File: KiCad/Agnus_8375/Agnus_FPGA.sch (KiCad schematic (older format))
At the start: 19 parts, among them J6 Conn_01x01, U1 10M02SCU169C8G, U2 LM1117-3.3

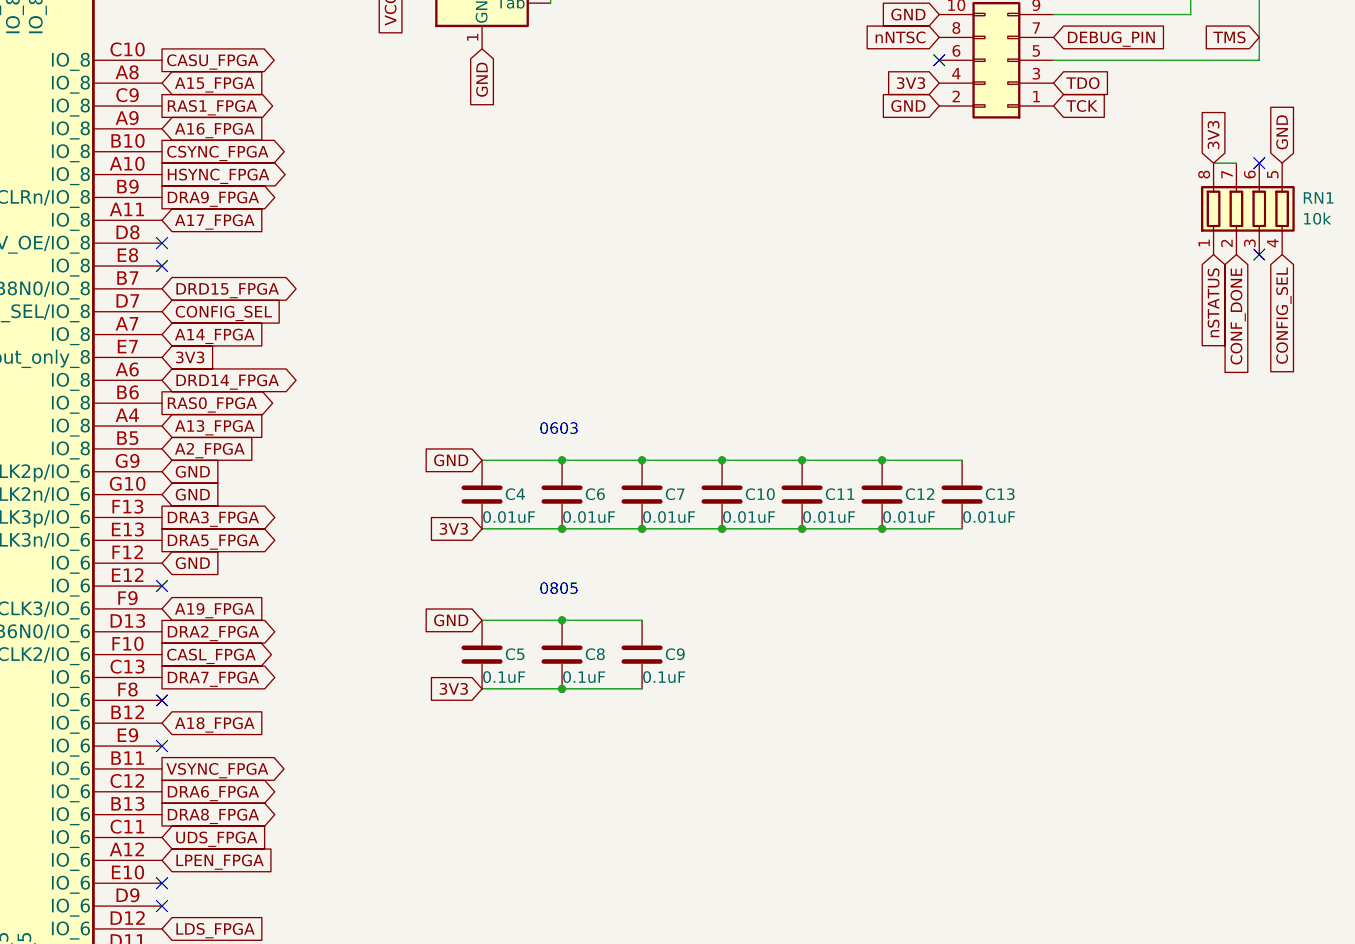
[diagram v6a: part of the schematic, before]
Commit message: Added more decoupling caps, changed to 6 mil copper pour clearance, added some more 3V3/GND vias, improved routing.
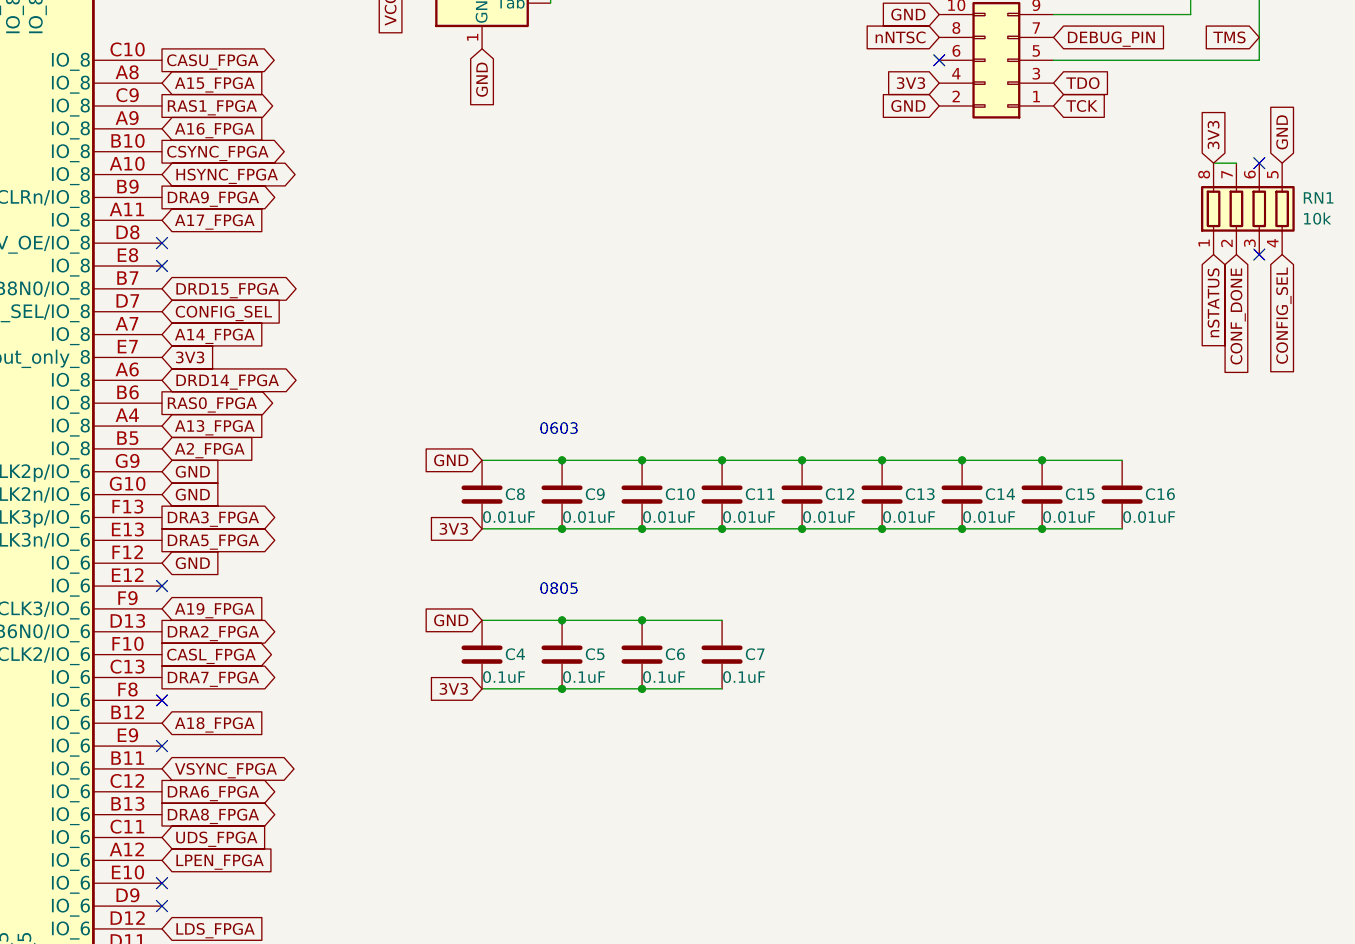
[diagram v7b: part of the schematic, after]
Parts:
- added C10, C13: 0.01uF, Capacitor_SMD:C_0603_1608Metric_Pad1.05x0.95mm_HandSolder, symbol Device:C
- added C6: 0.1uF, Capacitor_SMD:C_0805_2012Metric_Pad1.15x1.40mm_HandSolder, symbol Device:C
- renumbered C7 to C11, C10 to C12, C11 to C14, C12 to C15, C13 to C16, C5 to C4, C8 to C5, C9 to C7, C4 to C8, C6 to C9
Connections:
- net 3V3: now also C10.2, C13.2, C6.2
- net GND: now also C10.1, C13.1, C6.1
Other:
- moved on the sheet: C11, C12, C14, C15, C16, C7
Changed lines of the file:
@@
 Text GLabel 5850 2550 2    50   Input ~ 0
 A17_FPGA
-Text GLabel 5850 4950 2    50   Output ~ 0
+Text GLabel 5850 4950 2    50   BiDi ~ 0
 VSYNC_FPGA
 Text GLabel 5850 2250 2    50   Output ~ 0
 CSYNC_FPGA
-Text GLabel 5850 2350 2    50   Output ~ 0
+Text GLabel 5850 2350 2    50   BiDi ~ 0
 HSYNC_FPGA
 Text GLabel 5850 2150 2    50   Input ~ 0
@@
 L Device:C C?
 U 1 1 60CC8EF6
+P 10050 3750
+AR Path="/60CC8EF6" Ref="C?"  Part="1"
+AR Path="/608A10F5/60CC8EF6" Ref="C16"  Part="1"
+F 0 "C16" H 10150 3750 50  0000 L CNN
+F 1 "0.01uF" H 10050 3650 50  0000 L CNN
+F 2 "Capacitor_SMD:C_0603_1608Metric_Pad1.05x0.95mm_HandSolder" H 10088 3600 50  0001 C CNN
+F 3 "~" H 10050 3750 50  0001 C CNN
+	1    10050 3750
+	1    0    0    -1
+$EndComp
+$Comp
+L Device:C C?
+U 1 1 60CC8EFC
+P 9700 3750
+AR Path="/60CC8EFC" Ref="C?"  Part="1"
+AR Path="/608A10F5/60CC8EFC" Ref="C15"  Part="1"
+F 0 "C15" H 9800 3750 50  0000 L CNN
+F 1 "0.01uF" H 9700 3650 50  0000 L CNN
+F 2 "Capacitor_SMD:C_0603_1608Metric_Pad1.05x0.95mm_HandSolder" H 9738 3600 50  0001 C CNN
+F 3 "~" H 9700 3750 50  0001 C CNN
+	1    9700 3750
+	1    0    0    -1
+$EndComp
+$Comp
+L Device:C C?
+U 1 1 60CC8F02
 P 9350 3750
-AR Path="/60CC8EF6" Ref="C?"  Part="1"
-AR Path="/608A10F5/60CC8EF6" Ref="C13"  Part="1"
-F 0 "C13" H 9450 3750 50  0000 L CNN
+AR Path="/60CC8F02" Ref="C?"  Part="1"
+AR Path="/608A10F5/60CC8F02" Ref="C14"  Part="1"
+F 0 "C14" H 9450 3750 50  0000 L CNN
 F 1 "0.01uF" H 9350 3650 50  0000 L CNN
 F 2 "Capacitor_SMD:C_0603_1608Metric_Pad1.05x0.95mm_HandSolder" H 9388 3600 50  0001 C CNN
@@
 	1    0    0    -1
 $EndComp
-$Comp
-L Device:C C?
-U 1 1 60CC8EFC
-P 9000 3750
-AR Path="/60CC8EFC" Ref="C?"  Part="1"
-AR Path="/608A10F5/60CC8EFC" Ref="C12"  Part="1"
-F 0 "C12" H 9100 3750 50  0000 L CNN
-F 1 "0.01uF" H 9000 3650 50  0000 L CNN
-F 2 "Capacitor_SMD:C_0603_1608Metric_Pad1.05x0.95mm_HandSolder" H 9038 3600 50  0001 C CNN
-F 3 "~" H 9000 3750 50  0001 C CNN
-	1    9000 3750
-	1    0    0    -1
-$EndComp
-$Comp
-L Device:C C?
-U 1 1 60CC8F02
-P 8650 3750
-AR Path="/60CC8F02" Ref="C?"  Part="1"
-AR Path="/608A10F5/60CC8F02" Ref="C11"  Part="1"
-F 0 "C11" H 8750 3750 50  0000 L CNN
-F 1 "0.01uF" H 8650 3650 50  0000 L CNN
-F 2 "Capacitor_SMD:C_0603_1608Metric_Pad1.05x0.95mm_HandSolder" H 8688 3600 50  0001 C CNN
-F 3 "~" H 8650 3750 50  0001 C CNN
-	1    8650 3750
-	1    0    0    -1
-$EndComp
 Connection ~ 7600 3600
 Wire Wire Line
@@
 L Device:C C?
 U 1 1 60CC8F0E
-P 7950 4450
+P 8300 4450
 AR Path="/60CC8F0E" Ref="C?"  Part="1"
-AR Path="/608A10F5/60CC8F0E" Ref="C9"  Part="1"
-F 0 "C9" H 8050 4450 50  0000 L CNN
-F 1 "0.1uF" H 7950 4350 50  0000 L CNN
-F 2 "Capacitor_SMD:C_0805_2012Metric_Pad1.15x1.40mm_HandSolder" H 7988 4300 50  0001 C CNN
-F 3 "~" H 7950 4450 50  0001 C CNN
-	1    7950 4450
+AR Path="/608A10F5/60CC8F0E" Ref="C7"  Part="1"
+F 0 "C7" H 8400 4450 50  0000 L CNN
+F 1 "0.1uF" H 8300 4350 50  0000 L CNN
+F 2 "Capacitor_SMD:C_0805_2012Metric_Pad1.15x1.40mm_HandSolder" H 8338 4300 50  0001 C CNN
+F 3 "~" H 8300 4450 50  0001 C CNN
+	1    8300 4450
 	1    0    0    -1
 $EndComp
@@
 NoConn ~ 5850 2650
 NoConn ~ 5200 1250
-Wire Wire Line
-	8300 3600 8650 3600
 Connection ~ 8300 3600
 Wire Wire Line
-	8300 3900 8650 3900
-Connection ~ 8300 3900
+	9000 3900 9350 3900
 $Comp
 L Device:C C?
@@
 P 7600 4450
 AR Path="/607ACE36" Ref="C?"  Part="1"
-AR Path="/608A10F5/607ACE36" Ref="C8"  Part="1"
-F 0 "C8" H 7700 4450 50  0000 L CNN
+AR Path="/608A10F5/607ACE36" Ref="C5"  Part="1"
+F 0 "C5" H 7700 4450 50  0000 L CNN
 F 1 "0.1uF" H 7600 4350 50  0000 L CNN
 F 2 "Capacitor_SMD:C_0805_2012Metric_Pad1.15x1.40mm_HandSolder" H 7638 4300 50  0001 C CNN
@@
 $EndComp
 Wire Wire Line
-	9000 3600 8650 3600
-Connection ~ 8650 3600
-Wire Wire Line
-	9000 3900 8650 3900
-Connection ~ 8650 3900
+	9700 3900 9350 3900
+Connection ~ 9350 3900
 $Comp
 L Device:R_Pack04 RN2
@@
 P 7250 3750
 AR Path="/60636E2E" Ref="C?"  Part="1"
-AR Path="/608A10F5/60636E2E" Ref="C4"  Part="1"
-F 0 "C4" H 7350 3750 50  0000 L CNN
+AR Path="/608A10F5/60636E2E" Ref="C8"  Part="1"
+F 0 "C8" H 7350 3750 50  0000 L CNN
 F 1 "0.01uF" H 7250 3650 50  0000 L CNN
 F 2 "Capacitor_SMD:C_0603_1608Metric_Pad1.05x0.95mm_HandSolder" H 7288 3600 50  0001 C CNN
@@
 P 7600 3750
 AR Path="/60637476" Ref="C?"  Part="1"
-AR Path="/608A10F5/60637476" Ref="C6"  Part="1"
-F 0 "C6" H 7700 3750 50  0000 L CNN
+AR Path="/608A10F5/60637476" Ref="C9"  Part="1"
+F 0 "C9" H 7700 3750 50  0000 L CNN
 F 1 "0.01uF" H 7600 3650 50  0000 L CNN
 F 2 "Capacitor_SMD:C_0603_1608Metric_Pad1.05x0.95mm_HandSolder" H 7638 3600 50  0001 C CNN
@@
 L Device:C C?
 U 1 1 60637B30
-P 7950 3750
+P 8300 3750
 AR Path="/60637B30" Ref="C?"  Part="1"
-AR Path="/608A10F5/60637B30" Ref="C7"  Part="1"
-F 0 "C7" H 8050 3750 50  0000 L CNN
-F 1 "0.01uF" H 7950 3650 50  0000 L CNN
-F 2 "Capacitor_SMD:C_0603_1608Metric_Pad1.05x0.95mm_HandSolder" H 7988 3600 50  0001 C CNN
-F 3 "~" H 7950 3750 50  0001 C CNN
-	1    7950 3750
-	1    0    0    -1
-$EndComp
-$Comp
-L Device:C C?
-U 1 1 60638427
-P 8300 3750
-AR Path="/60638427" Ref="C?"  Part="1"
-AR Path="/608A10F5/60638427" Ref="C10"  Part="1"
-F 0 "C10" H 8400 3750 50  0000 L CNN
+AR Path="/608A10F5/60637B30" Ref="C11"  Part="1"
+F 0 "C11" H 8400 3750 50  0000 L CNN
 F 1 "0.01uF" H 8300 3650 50  0000 L CNN
 F 2 "Capacitor_SMD:C_0603_1608Metric_Pad1.05x0.95mm_HandSolder" H 8338 3600 50  0001 C CNN
@@
 	1    0    0    -1
 $EndComp
-Wire Wire Line
-	9000 3600 9350 3600
-Connection ~ 9000 3600
-Wire Wire Line
-	9000 3900 9350 3900
-Connection ~ 9000 3900
+$Comp
+L Device:C C?
+U 1 1 60638427
+P 8650 3750
+AR Path="/60638427" Ref="C?"  Part="1"
+AR Path="/608A10F5/60638427" Ref="C12"  Part="1"
+F 0 "C12" H 8750 3750 50  0000 L CNN
+F 1 "0.01uF" H 8650 3650 50  0000 L CNN
+F 2 "Capacitor_SMD:C_0603_1608Metric_Pad1.05x0.95mm_HandSolder" H 8688 3600 50  0001 C CNN
+F 3 "~" H 8650 3750 50  0001 C CNN
+	1    8650 3750
+	1    0    0    -1
+$EndComp
+Wire Wire Line
+	9700 3900 10050 3900
+Connection ~ 9700 3900
 Wire Wire Line
 	7250 3900 7600 3900
@@
 P 7250 4450
 AR Path="/60785965" Ref="C?"  Part="1"
-AR Path="/608A10F5/60785965" Ref="C5"  Part="1"
-F 0 "C5" H 7350 4450 50  0000 L CNN
+AR Path="/608A10F5/60785965" Ref="C4"  Part="1"
+F 0 "C4" H 7350 4450 50  0000 L CNN
 F 1 "0.1uF" H 7250 4350 50  0000 L CNN
 F 2 "Capacitor_SMD:C_0805_2012Metric_Pad1.15x1.40mm_HandSolder" H 7288 4300 50  0001 C CNN
@@
 Text GLabel 950  1950 0    50   Input ~ 0
 DEBUG_PIN
+$Comp
+L Device:C C?
+U 1 1 608291F3
+P 7950 4450
+AR Path="/608291F3" Ref="C?"  Part="1"
+AR Path="/608A10F5/608291F3" Ref="C6"  Part="1"
+F 0 "C6" H 8050 4450 50  0000 L CNN
+F 1 "0.1uF" H 7950 4350 50  0000 L CNN
+F 2 "Capacitor_SMD:C_0805_2012Metric_Pad1.15x1.40mm_HandSolder" H 7988 4300 50  0001 C CNN
+F 3 "~" H 7950 4450 50  0001 C CNN
+	1    7950 4450
+	1    0    0    -1
+$EndComp
+Wire Wire Line
+	7950 4300 8300 4300
+Connection ~ 7950 4300
+Wire Wire Line
+	7950 4600 8300 4600
+Connection ~ 7950 4600
+$Comp
+L Device:C C?
+U 1 1 60898D1D
+P 9000 3750
+AR Path="/60898D1D" Ref="C?"  Part="1"
+AR Path="/608A10F5/60898D1D" Ref="C13"  Part="1"
+F 0 "C13" H 9100 3750 50  0000 L CNN
+F 1 "0.01uF" H 9000 3650 50  0000 L CNN
+F 2 "Capacitor_SMD:C_0603_1608Metric_Pad1.05x0.95mm_HandSolder" H 9038 3600 50  0001 C CNN
+F 3 "~" H 9000 3750 50  0001 C CNN
+	1    9000 3750
+	1    0    0    -1
+$EndComp
+Wire Wire Line
+	9350 3600 9700 3600
+Connection ~ 9350 3600
+Wire Wire Line
+	8300 3600 8650 3600
+Connection ~ 8650 3600
+Wire Wire Line
+	8650 3600 9000 3600
+$Comp
+L Device:C C?
+U 1 1 608A7236
+P 7950 3750
+AR Path="/608A7236" Ref="C?"  Part="1"
+AR Path="/608A10F5/608A7236" Ref="C10"  Part="1"
+F 0 "C10" H 8050 3750 50  0000 L CNN
+F 1 "0.01uF" H 7950 3650 50  0000 L CNN
+F 2 "Capacitor_SMD:C_0603_1608Metric_Pad1.05x0.95mm_HandSolder" H 7988 3600 50  0001 C CNN
+F 3 "~" H 7950 3750 50  0001 C CNN
+	1    7950 3750
+	1    0    0    -1
+$EndComp
+Connection ~ 9000 3600
+Wire Wire Line
+	9000 3600 9350 3600
+Wire Wire Line
+	10050 3600 9700 3600
+Connection ~ 9700 3600
+Wire Wire Line
+	8300 3900 8650 3900
+Connection ~ 8300 3900
+Connection ~ 9000 3900
+Connection ~ 8650 3900
+Wire Wire Line
+	8650 3900 9000 3900
 $EndSCHEMATC
